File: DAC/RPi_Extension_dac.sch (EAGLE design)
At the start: 33 parts, among them U1 AD5360BSTZ, U2 ADR423ARZ

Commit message: updated pcbs
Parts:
- C1, C10, C12, C13, C15, C16, C2, C6, C8: value (none) -> 100nF
- C11, C14, C17, C3, C4, C5, C7, C9: value (none) -> 10uF
- R1, R2: value (none) -> 100k
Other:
- moved on the sheet: C16, C17
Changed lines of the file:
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@@
 <part name="GND" library="supply1" deviceset="GND" device=""/>
 <part name="SV1" library="con-lstb" deviceset="MA08-2W" device=""/>
-<part name="C1" library="rcl" deviceset="C-EU" device="C0603"/>
-<part name="C2" library="rcl" deviceset="C-EU" device="C0603"/>
-<part name="C3" library="rcl" deviceset="C-EU" device="C1206"/>
-<part name="C4" library="rcl" deviceset="C-EU" device="C1206"/>
+<part name="C1" library="rcl" deviceset="C-EU" device="C0603" value="100nF"/>
+<part name="C2" library="rcl" deviceset="C-EU" device="C0603" value="100nF"/>
+<part name="C3" library="rcl" deviceset="C-EU" device="C1206" value="10uF"/>
+<part name="C4" library="rcl" deviceset="C-EU" device="C1206" value="10uF"/>
 <part name="GND1" library="supply1" deviceset="GND" device=""/>
 <part name="GND2" library="supply1" deviceset="GND" device=""/>
-<part name="C5" library="rcl" deviceset="C-EU" device="C1206"/>
-<part name="C6" library="rcl" deviceset="C-EU" device="C0603"/>
-<part name="C7" library="rcl" deviceset="C-EU" device="C1206"/>
-<part name="C8" library="rcl" deviceset="C-EU" device="C0603"/>
+<part name="C5" library="rcl" deviceset="C-EU" device="C1206" value="10uF"/>
+<part name="C6" library="rcl" deviceset="C-EU" device="C0603" value="100nF"/>
+<part name="C7" library="rcl" deviceset="C-EU" device="C1206" value="10uF"/>
+<part name="C8" library="rcl" deviceset="C-EU" device="C0603" value="100nF"/>
 <part name="GND3" library="supply1" deviceset="GND" device=""/>
-<part name="C9" library="rcl" deviceset="C-EU" device="C1206"/>
-<part name="C10" library="rcl" deviceset="C-EU" device="C0603"/>
-<part name="C11" library="rcl" deviceset="C-EU" device="C1206"/>
-<part name="C12" library="rcl" deviceset="C-EU" device="C0603"/>
+<part name="C9" library="rcl" deviceset="C-EU" device="C1206" value="10uF"/>
+<part name="C10" library="rcl" deviceset="C-EU" device="C0603" value="100nF"/>
+<part name="C11" library="rcl" deviceset="C-EU" device="C1206" value="10uF"/>
+<part name="C12" library="rcl" deviceset="C-EU" device="C0603" value="100nF"/>
 <part name="GND4" library="supply1" deviceset="GND" device=""/>
 <part name="SV3" library="con-lsta" deviceset="FE08-2" device=""/>
@@
 <part name="U2" library="ADR423ARZ" deviceset="ADR423ARZ" device=""/>
 <part name="GND7" library="supply1" deviceset="GND" device=""/>
-<part name="C13" library="rcl" deviceset="C-EU" device="C0603"/>
-<part name="C14" library="rcl" deviceset="C-EU" device="C1206"/>
+<part name="C13" library="rcl" deviceset="C-EU" device="C0603" value="100nF"/>
+<part name="C14" library="rcl" deviceset="C-EU" device="C1206" value="10uF"/>
 <part name="GND8" library="supply1" deviceset="GND" device=""/>
-<part name="C15" library="rcl" deviceset="C-EU" device="C0603"/>
-<part name="C16" library="rcl" deviceset="C-EU" device="C0603"/>
-<part name="C17" library="rcl" deviceset="C-EU" device="C1206"/>
+<part name="C15" library="rcl" deviceset="C-EU" device="C0603" value="100nF"/>
+<part name="C16" library="rcl" deviceset="C-EU" device="C0603" value="100nF"/>
+<part name="C17" library="rcl" deviceset="C-EU" device="C1206" value="10uF"/>
 <part name="GND9" library="supply1" deviceset="GND" device=""/>
 <part name="SV2" library="con-lstb" deviceset="MA08-2W" device=""/>
@@
 <part name="GND11" library="supply1" deviceset="GND" device=""/>
 <part name="GND12" library="supply1" deviceset="GND" device=""/>
-<part name="R1" library="resistor" deviceset="R-EU_" device="R0603"/>
-<part name="R2" library="resistor" deviceset="R-EU_" device="R0603"/>
+<part name="R1" library="resistor" deviceset="R-EU_" device="R0603" value="100k"/>
+<part name="R2" library="resistor" deviceset="R-EU_" device="R0603" value="100k"/>
 </parts>
 <sheets>
@@
 <instance part="GND8" gate="1" x="317.5" y="91.44"/>
 <instance part="C15" gate="G$1" x="317.5" y="111.76"/>
-<instance part="C16" gate="G$1" x="325.12" y="111.76"/>
-<instance part="C17" gate="G$1" x="332.74" y="111.76"/>
+<instance part="C16" gate="G$1" x="330.2" y="111.76"/>
+<instance part="C17" gate="G$1" x="340.36" y="111.76"/>
 <instance part="GND9" gate="1" x="213.36" y="66.04" rot="R90"/>
 <instance part="SV2" gate="1" x="205.74" y="50.8" rot="R180"/>
@@
 <junction x="317.5" y="96.52"/>
 <pinref part="C16" gate="G$1" pin="2"/>
-<wire x1="325.12" y1="106.68" x2="317.5" y2="106.68" width="0.1524" layer="91"/>
+<wire x1="330.2" y1="106.68" x2="317.5" y2="106.68" width="0.1524" layer="91"/>
 <junction x="317.5" y="106.68"/>
 <pinref part="C17" gate="G$1" pin="2"/>
-<wire x1="332.74" y1="106.68" x2="325.12" y2="106.68" width="0.1524" layer="91"/>
-<junction x="325.12" y="106.68"/>
+<wire x1="340.36" y1="106.68" x2="330.2" y2="106.68" width="0.1524" layer="91"/>
+<junction x="330.2" y="106.68"/>
 </segment>
 <segment>
@@
 <pinref part="U2" gate="A" pin="VOUT"/>
 <wire x1="309.88" y1="116.84" x2="317.5" y2="116.84" width="0.1524" layer="91"/>
-<label x="337.82" y="116.84" size="1.778" layer="95"/>
+<label x="345.44" y="116.84" size="1.778" layer="95"/>
 <pinref part="C15" gate="G$1" pin="1"/>
 <wire x1="317.5" y1="114.3" x2="317.5" y2="116.84" width="0.1524" layer="91"/>
 <junction x="317.5" y="116.84"/>
-<wire x1="317.5" y1="116.84" x2="325.12" y2="116.84" width="0.1524" layer="91"/>
+<wire x1="317.5" y1="116.84" x2="330.2" y2="116.84" width="0.1524" layer="91"/>
 <pinref part="C17" gate="G$1" pin="1"/>
-<wire x1="325.12" y1="116.84" x2="332.74" y2="116.84" width="0.1524" layer="91"/>
-<wire x1="332.74" y1="114.3" x2="332.74" y2="116.84" width="0.1524" layer="91"/>
+<wire x1="330.2" y1="116.84" x2="340.36" y2="116.84" width="0.1524" layer="91"/>
+<wire x1="340.36" y1="114.3" x2="340.36" y2="116.84" width="0.1524" layer="91"/>
 <pinref part="C16" gate="G$1" pin="1"/>
-<wire x1="325.12" y1="114.3" x2="325.12" y2="116.84" width="0.1524" layer="91"/>
-<junction x="325.12" y="116.84"/>
-<wire x1="332.74" y1="116.84" x2="337.82" y2="116.84" width="0.1524" layer="91"/>
-<junction x="332.74" y="116.84"/>
-</segment>
-</net>
+<wire x1="330.2" y1="114.3" x2="330.2" y2="116.84" width="0.1524" layer="91"/>
+<junction x="330.2" y="116.84"/>
+<wire x1="340.36" y1="116.84" x2="345.44" y2="116.84" width="0.1524" layer="91"/>
+<junction x="340.36" y="116.84"/>
+</segment>
+</net>

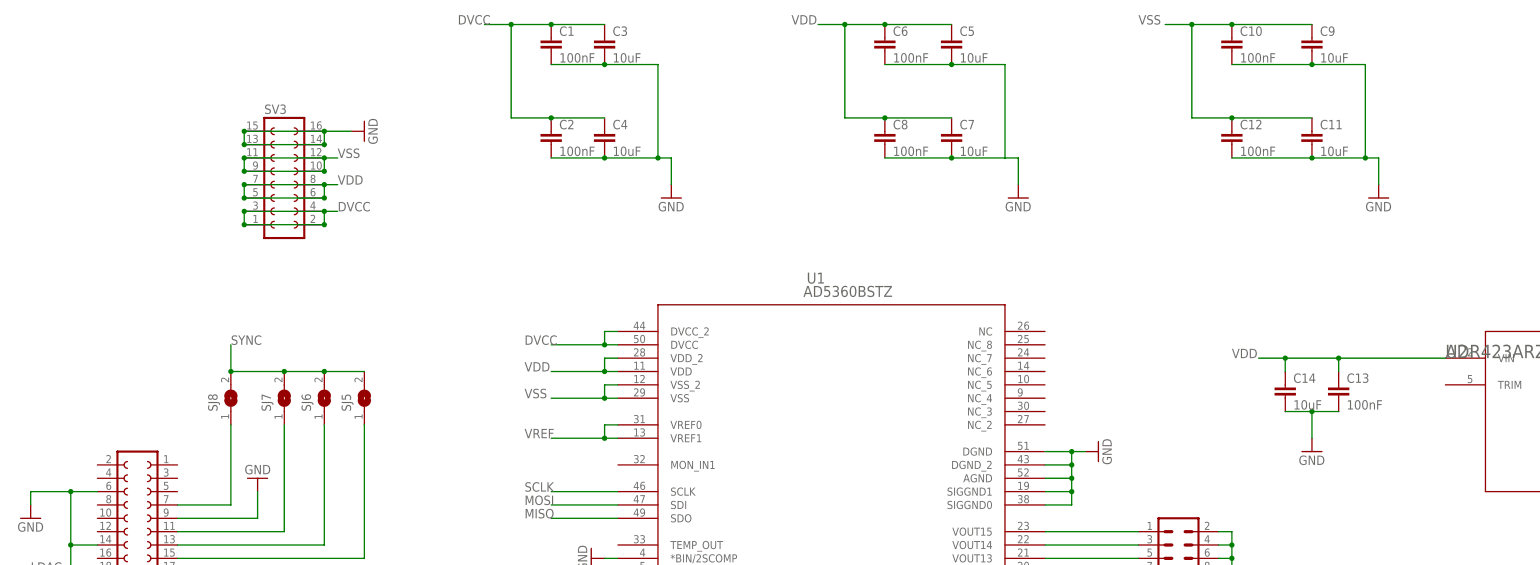
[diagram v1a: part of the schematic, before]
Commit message: used consistent naming and units for values
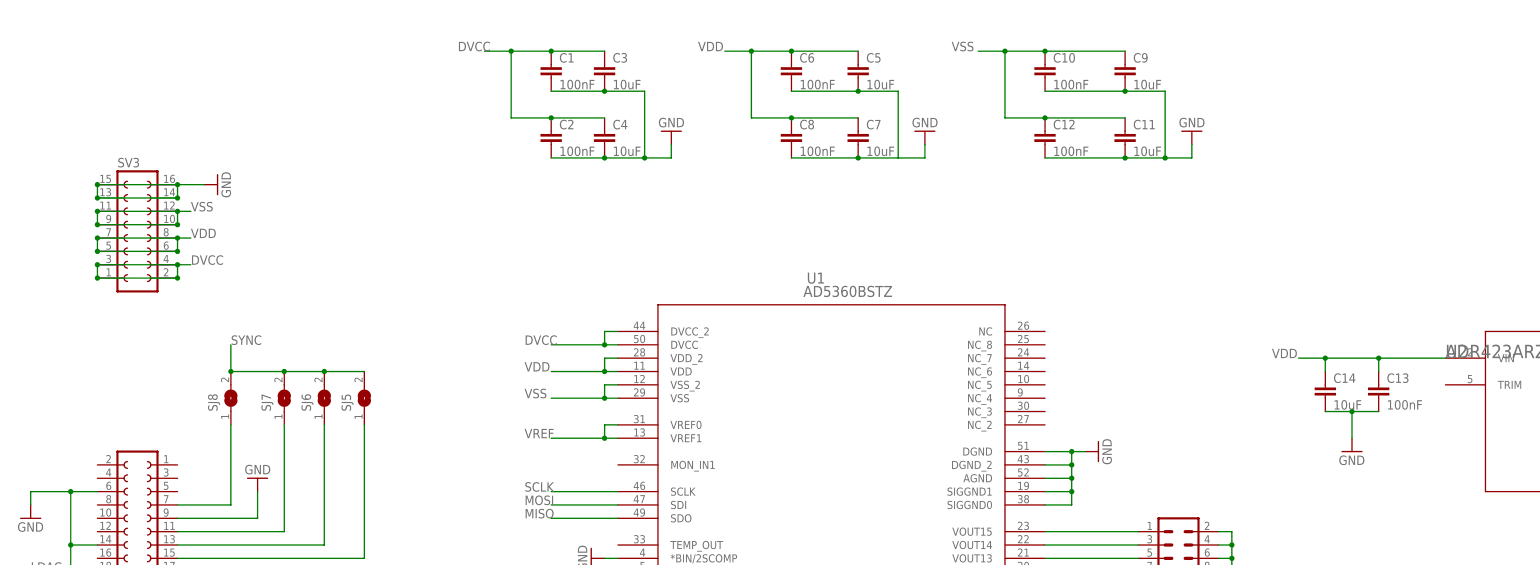
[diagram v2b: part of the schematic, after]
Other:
- moved on the sheet: C1, C10, C11, C12, C13, C14, C3, C5, C6, C7, C8, C9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

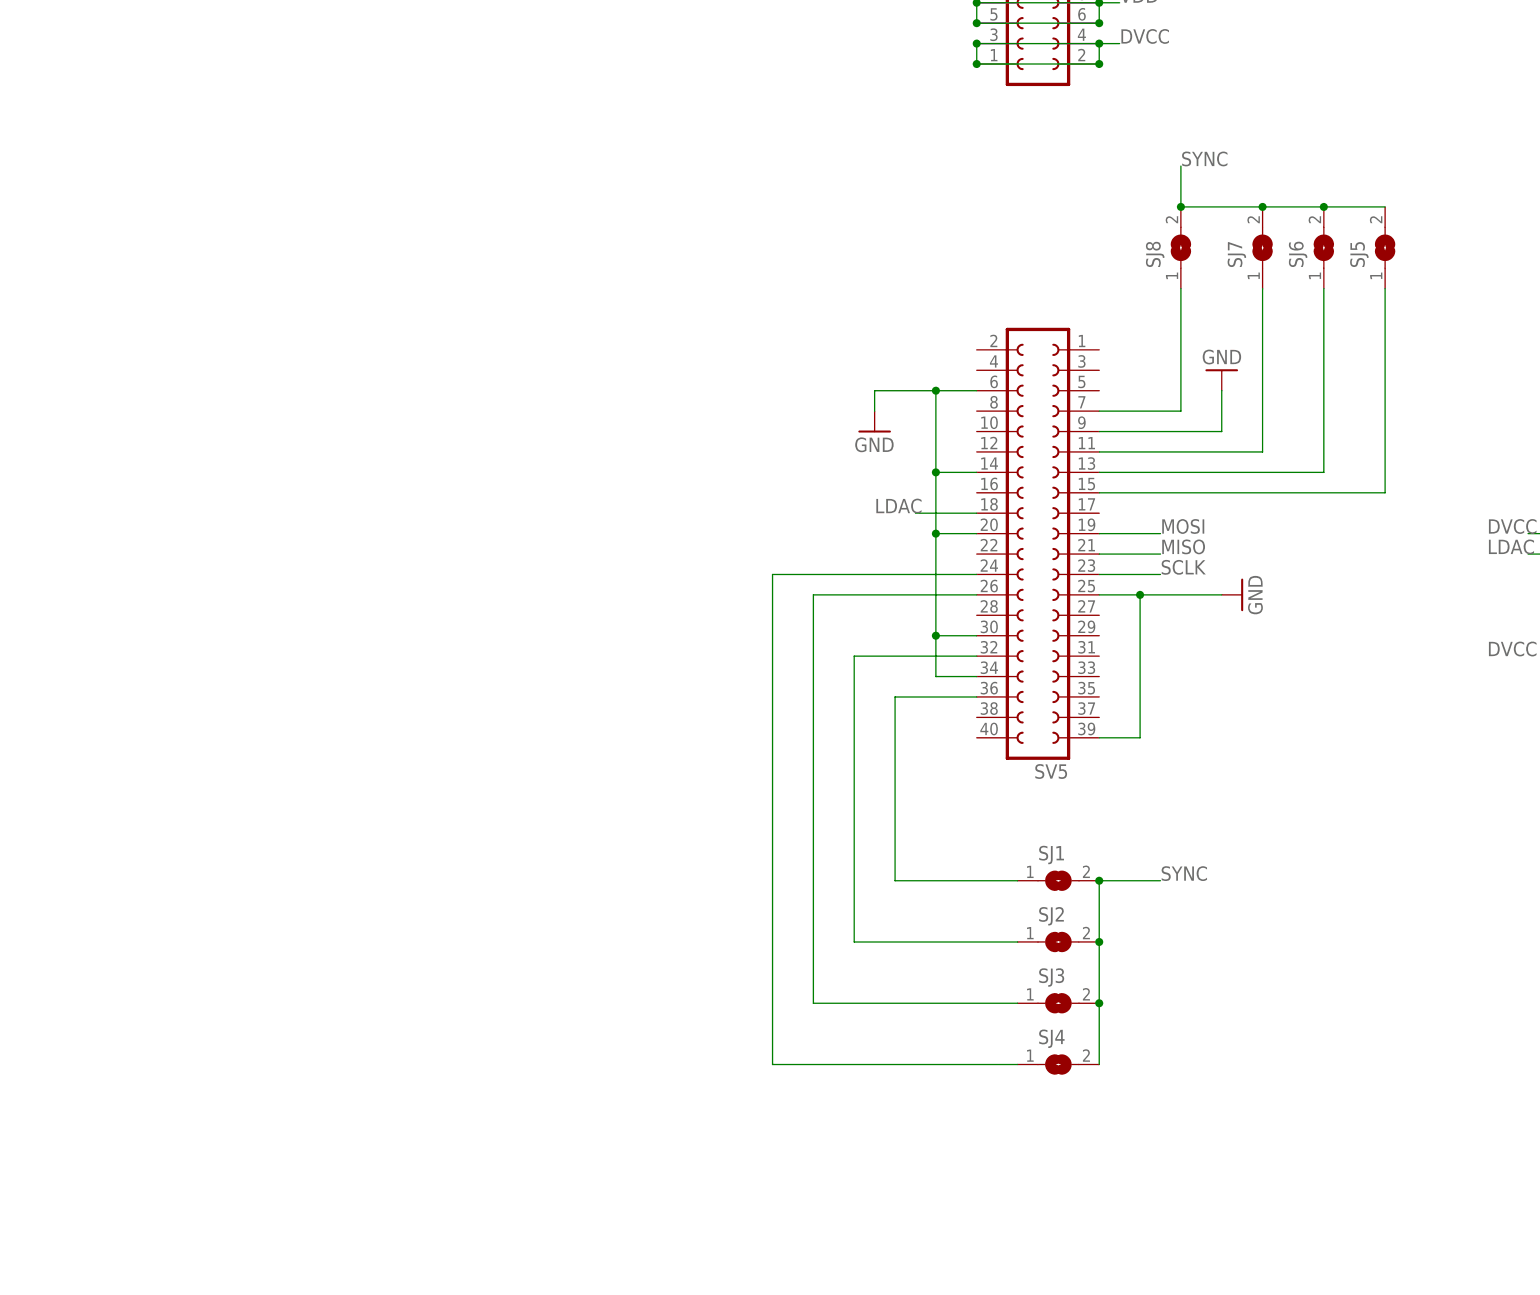
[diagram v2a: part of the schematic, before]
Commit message: added additional id jumpers to adc and dac board
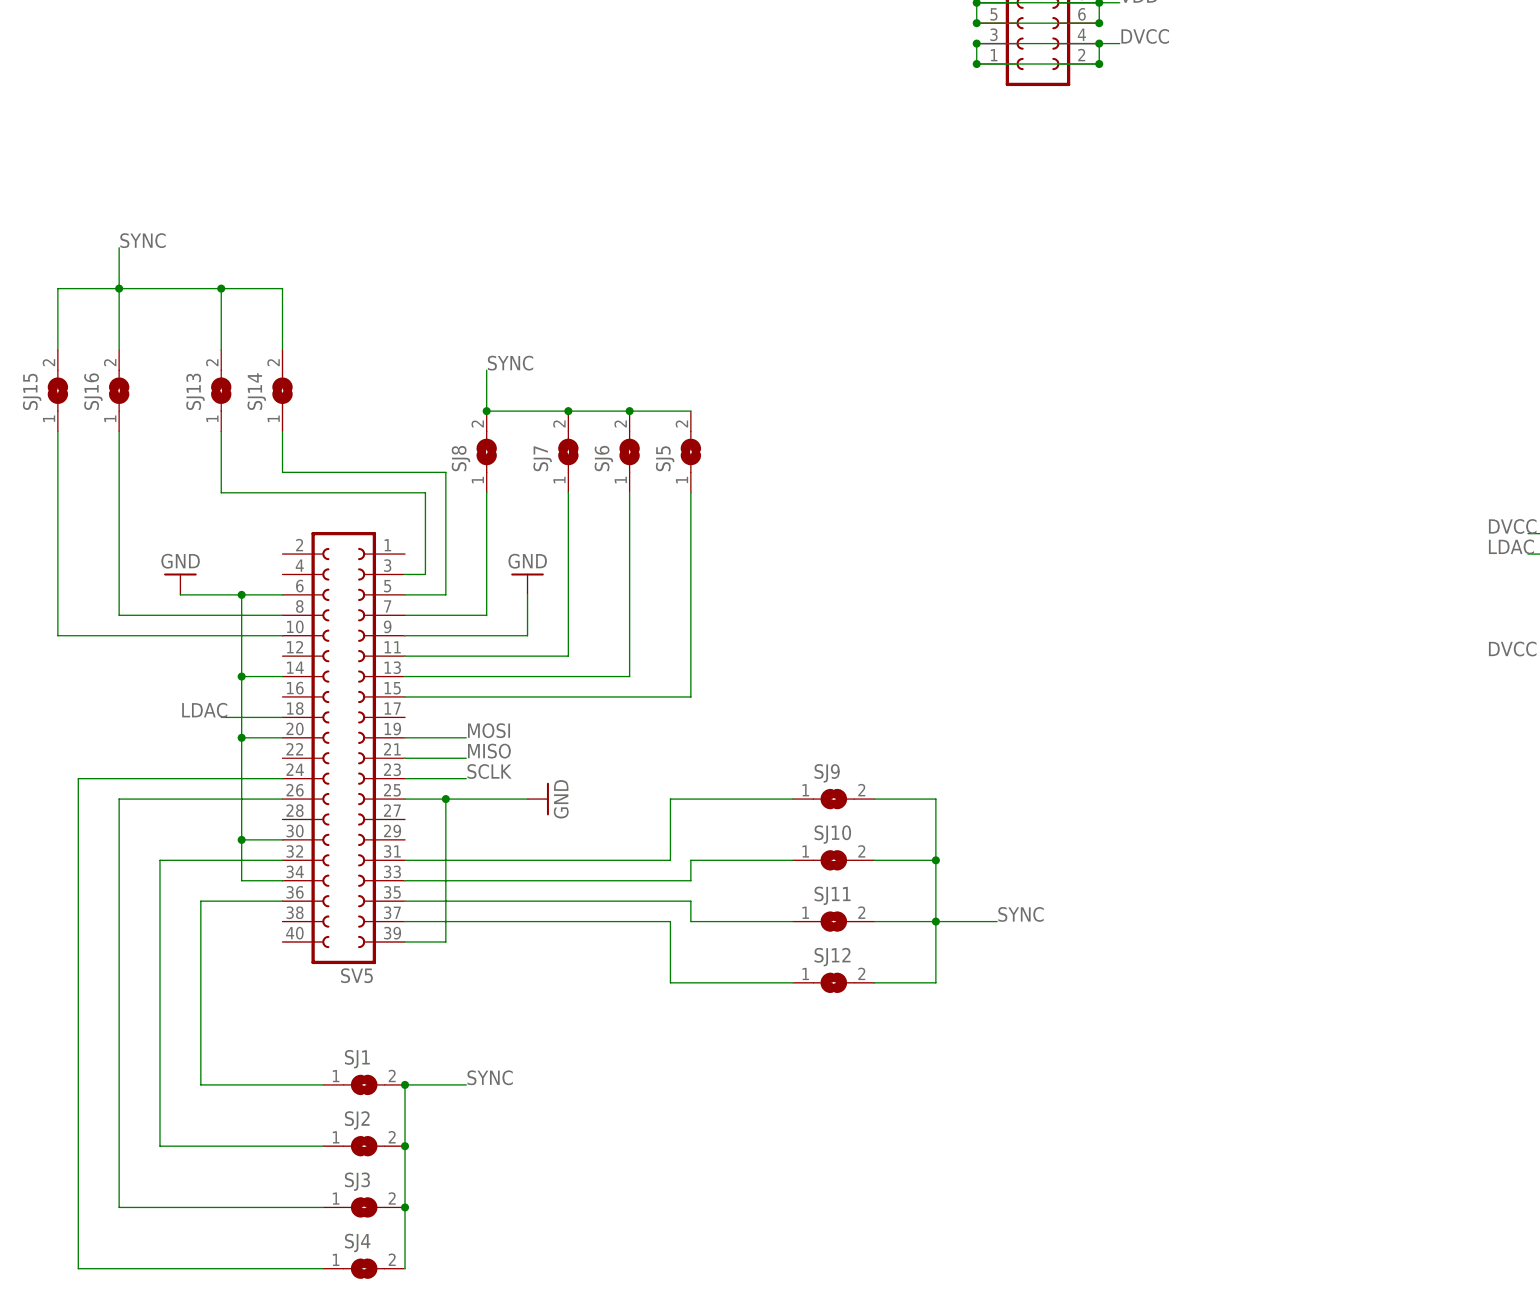
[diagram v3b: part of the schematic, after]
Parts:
- added SJ10, SJ11, SJ12, SJ13, SJ14, SJ15, SJ16, SJ9: (no value), jumper:SJ
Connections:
- new net N$19: SJ9.1, SV5.31
- new net N$28: SJ10.1, SV5.33
- new net N$29: SJ11.1, SV5.35
- new net N$30: SJ12.1, SV5.37
- new net N$31: SJ13.1, SV5.3
- new net N$32: SJ14.1, SV5.5
- new net N$33: SJ16.1, SV5.8
- new net N$34: SJ15.1, SV5.10
- net SYNC: now also SJ10.2, SJ11.2, SJ12.2, SJ13.2, SJ14.2, SJ15.2, SJ16.2, SJ9.2
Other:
- moved on the sheet: SJ1, SJ2, SJ3, SJ4, SJ5, SJ6, SJ7, SJ8, SV5
